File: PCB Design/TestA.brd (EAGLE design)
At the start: 50 x 50 mm, 52 parts, among them IC1 SI7021, IC2 ATMEGA328-PB, IC3 PE4259, U1 V_REG_317SMD, U2 LSM9DS1, Y1 16MHz, Y2 32Mhz

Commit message: Completed first iteration of this board
Ready for QA
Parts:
- moved A1 11.7 mm to (8.45, 10.2), turned to 180 degrees
- moved C13 6.55 mm to (26.1, 34.9)
- moved C12 3.93 mm to (22.2, 34.9), turned to 0 degrees
- moved L5 1.55 mm to (11.7, 16.6)
- moved C27 1.55 mm to (14.2, 16.6)
- moved C29 1.55 mm to (14.2, 17.9)
- moved C31 1.55 mm to (14.2, 15.2)
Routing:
- net N$22: track 10.6 -> 25.6 mm, vias 2 -> 3
- net N$15: track 15.0 -> 7.24 mm
- net N$8: track 7.83 -> 2.30 mm
- net GND: track 59.8 -> 64.1 mm, vias 23 -> 22
- net N$9: track 9.59 -> 7.67 mm
- net N$16: track 5.81 -> 4.32 mm
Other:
- board size 50 x 50 mm -> 41.8 x 43.6 mm

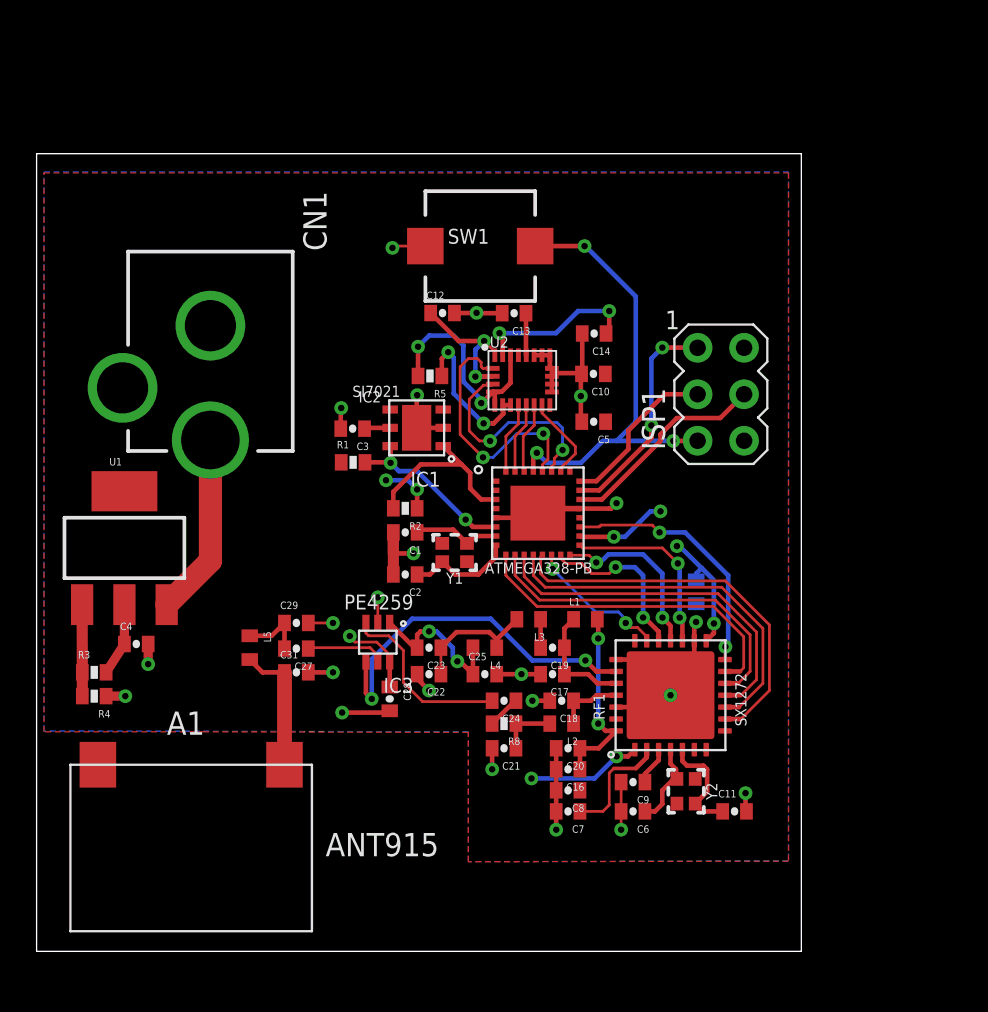
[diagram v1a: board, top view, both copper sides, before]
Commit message: Removed SMD Antenna and made a few other changes after preliminary QA
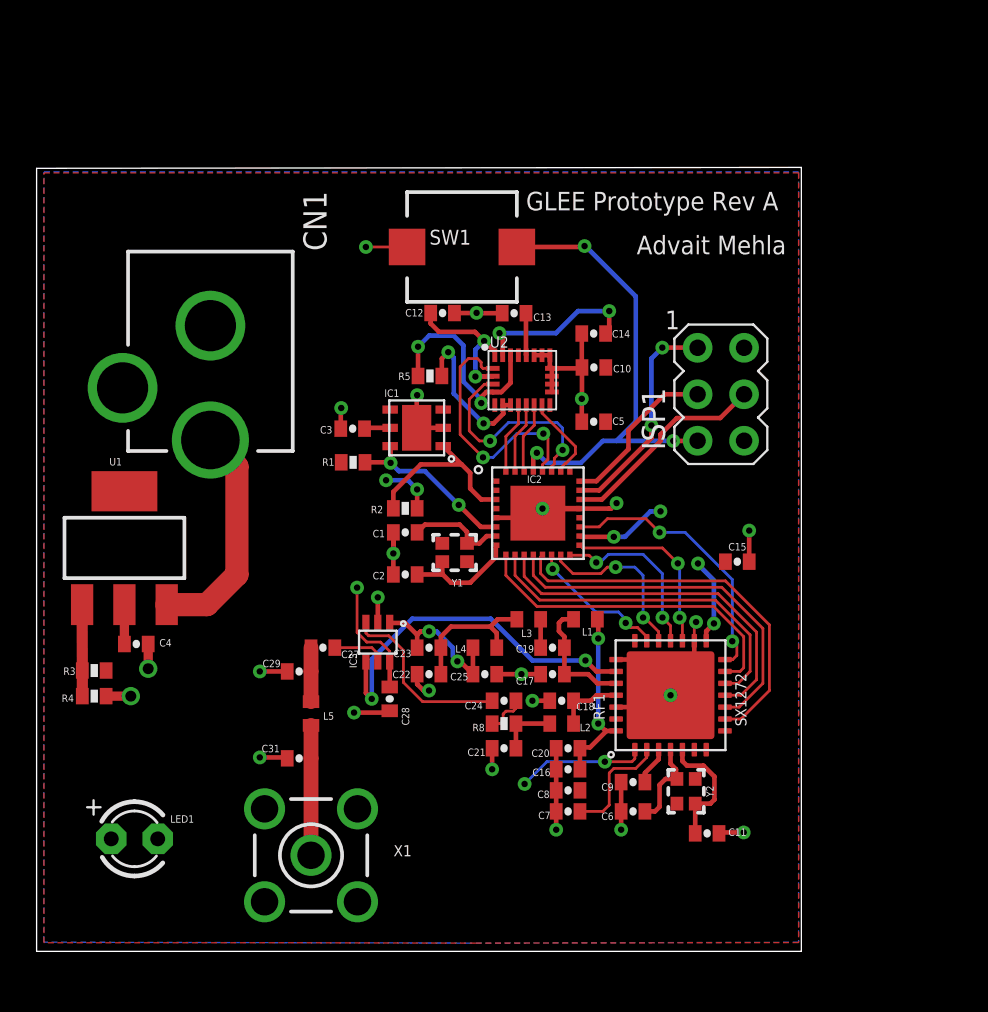
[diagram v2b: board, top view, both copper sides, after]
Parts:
- removed A1: ANT915, Mini-Project:ANT915
- added LED1: (no value), adafruit:LED3MM
- added X1: LTI-SASF54GT, con-coax:LTI-SASF54GT
- moved L5 4.92 mm to (15.0, 13.0)
- moved C31 4.70 mm to (14.3, 10.6), turned to 180 degrees
- moved C15 2.79 mm to (38.3, 21.3), flipped to the top, turned to 0 degrees
- moved C29 2.65 mm to (14.3, 15.3), turned to 180 degrees
- moved C11 1.92 mm to (36.6, 6.45)
- moved C27 1.45 mm to (15.7, 16.6)
- moved SW1 1.00 mm to (23.2, 38.5)
- moved C10 0.35 mm to (30.5, 31.9)
- moved R3 0.10 mm to (3.15, 15.3)
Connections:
- removed net 3.3V: C4.1, R3.2, U1.2
- net +3.3V: now also C4.1, LED1.A, R3.2, U1.2
- net GND: now also LED1.K, X1.2, X1.3, X1.4, X1.5
- net N$15: now also X1.1; no longer A1.1
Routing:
- net 3.3V: track 4.00 -> 0.00 mm
- net N$3: track 9.99 -> 12.5 mm
- net +3.3V: track 39.6 -> 41.9 mm
- net GND: track 64.1 -> 66.2 mm, vias 22 -> 24
- net N$16: track 4.32 -> 2.91 mm
- net N$22: track 25.6 -> 26.6 mm
- net DIO5: track 14.0 -> 14.9 mm
- net N$12: track 7.02 -> 7.89 mm
- net XTB: track 6.00 -> 6.77 mm
- net N$18: track 3.59 -> 2.95 mm
- net N$11: track 6.24 -> 6.84 mm
- net XTAL1: track 4.84 -> 5.43 mm
- net N$2: track 10.4 -> 9.83 mm
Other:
- board size 41.8 x 43.6 mm -> 41.8 x 42.9 mm
- board text added: "Advait Mehla"
- board text added: "GLEE Prototype Rev A"
